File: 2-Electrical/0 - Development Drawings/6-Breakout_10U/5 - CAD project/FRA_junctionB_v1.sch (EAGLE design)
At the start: 24 parts, among them U1 SSW-103-01-F-D, U10 SSW-103-01-F-D, U11 TB003V-500-P05BE, U12 TB003V-500-P10BE, U13 TB003V-500-P05BE, U14 TB003V-500-P10BE, U2 SSW-103-01-F-D, U3 SSW-103-01-F-D, U4 SSW-103-01-F-D, U5 SSW-103-01-F-D, U6 SSW-103-01-F-D, U7 SSW-103-01-F-D, U8 SSW-103-01-F-D, U9 SSW-103-01-F-D

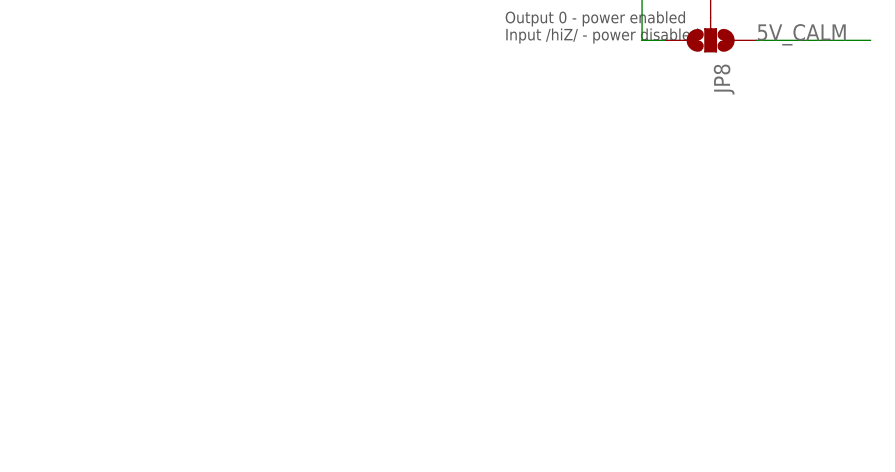
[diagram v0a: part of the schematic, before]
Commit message: silkscreen edits on breakout boards
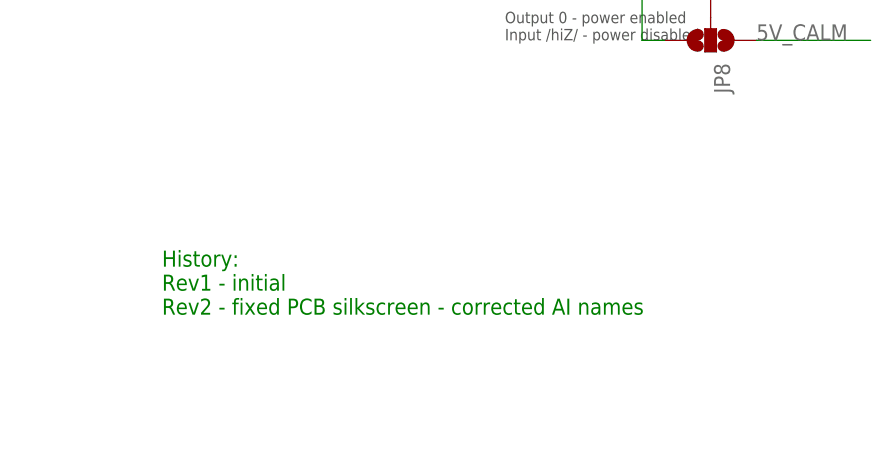
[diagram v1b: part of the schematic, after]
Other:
- note added: "History: Rev1 - initial Rev2 - fixed PCB silkscreen - corrected AI names"
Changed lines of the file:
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@@
 <?xml version="1.0" encoding="utf-8"?>
 <!DOCTYPE eagle SYSTEM "eagle.dtd">
-<eagle version="9.5.2">
+<eagle version="9.6.2">
 <drawing>
 <settings>
@@
 <attributes>
 <attribute name="CNAME" value="FRA Junction Board"/>
-<attribute name="CREVISION" value="01"/>
+<attribute name="CREVISION" value="02"/>
 </attributes>
 <variantdefs>
@@
 <text x="162.56" y="58.42" size="1.27" layer="97">Output 0 - power enabled
 Input /hiZ/ - power disabled</text>
+<text x="124.46" y="27.94" size="1.778" layer="91">History:
+Rev1 - initial
+Rev2 - fixed PCB silkscreen - corrected AI names</text>
 </plain>
 <instances>
